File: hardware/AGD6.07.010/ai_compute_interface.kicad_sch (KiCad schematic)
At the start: 12 parts, among them J1 AI_SIGNALS JST-GH 8, J2 AI_OFF_SWITCH JST-GH 2, U2 TPD4E05U06DQA

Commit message: Draw full AGD6.07.010 schematic per integrated_avionics_board spec
All ten sheets now carry components: 14S input with hot-swap and power
monitor, 12/5/3.3 V rails and a separate 12 V AI channel with soft-start
and current telemetry, Pixhawk connectors, CAN1/CAN2 hub with chokes,
ESD and switchable termination, sensor conditioning, SIYI and radar,
AI interface and watchdog, protected 12 V switches with diagnostics,
fan/heater control, cameras and Ethernet. Open choices are recorded in
DECISIONS.md; datasheet-dependent values are flagged CHECK_DATASHEET.

ERC: no errors. All 752 intended pin connections match the KiCad netlist.

Co-Authored-By: Claude Opus 5.5 <noreply@anthropic.com>
Claude-Session: https://claude.ai/code/session_01Qk7uTKdi6YbndB9fGuguYV
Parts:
- removed D1, D2: ESD9B5.0ST5G, Diode_SMD:D_SOD-923, symbol Diode:ESD9B5.0ST5G
- removed J1: AI_SIGNALS JST-GH 8, Connector_JST:JST_GH_SM08B-GHS-TB_1x08-1MP_P1.25mm_Horizontal, symbol Connector_Generic:Conn_01x08
- removed J2: AI_OFF_SWITCH JST-GH 2, Connector_JST:JST_GH_SM02B-GHS-TB_1x02-1MP_P1.25mm_Horizontal, symbol Connector_Generic:Conn_01x02
- removed R1, R2, R3, R4, R5, R9: 100, Resistor_SMD:R_0402_1005Metric, symbol Device:R
- removed R6: 100k, Resistor_SMD:R_0402_1005Metric, symbol Device:R
- removed U2: TPD4E05U06DQA, Package_SON:USON-10_2.5x1.0mm_P0.5mm, symbol Power_Protection:TPD4E05U06DQA
- added D601, D602: ESD9B5.0ST5G, Diode_SMD:D_SOD-923, symbol Diode:ESD9B5.0ST5G
- added J601: AI_SIGNALS GH8, Connector_JST:JST_GH_SM08B-GHS-TB_1x08-1MP_P1.25mm_Horizontal, symbol Connector_Generic:Conn_01x08
- added J602: AI_OFF_SWITCH GH2, Connector_JST:JST_GH_SM02B-GHS-TB_1x02-1MP_P1.25mm_Horizontal, symbol Connector_Generic:Conn_01x02
- added J603: SERVICE USB-C, Connector_USB:USB_C_Receptacle_GCT_USB4105-xx-A_16P_TopMnt_Horizontal, symbol Connector:USB_C_Receptacle_USB2.0_16P
- added J604: AI_USB GH4, Connector_JST:JST_GH_SM04B-GHS-TB_1x04-1MP_P1.25mm_Horizontal, symbol Connector_Generic:Conn_01x04
- added R601, R602, R603, R604, R605, R607: 100, Resistor_SMD:R_0402_1005Metric, symbol Device:R
- added R606: 100k, Resistor_SMD:R_0402_1005Metric, symbol Device:R
- added R608, R609: 5.1k, Resistor_SMD:R_0402_1005Metric, symbol Device:R
- added U602: TPD4E05U06DQA, Package_SON:USON-10_2.5x1.0mm_P0.5mm, symbol Power_Protection:TPD4E05U06DQA
- added U603: USBLC6-2SC6, Package_TO_SOT_SMD:SOT-23-6, symbol Power_Protection:USBLC6-2SC6
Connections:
- net AI_PWR_EN: now also R607.1
- net AI_RX: now also R602.1
- net AI_RX_C: now also J601.3 (Pin_3), R602.2, U602.2 (D1-)
- net AI_TX: now also R601.2
- net AI_TX_C: now also J601.2 (Pin_2), R601.1, U602.1 (D1+)
- net AI_WDI: now also R604.2
- net AI_WD_ARM: now also R605.2, R606.1
- net ARM_C: now also D601.1 (A1), J601.7 (Pin_7), R605.1
- net GND: now also D601.2 (A2), D602.2 (A2), J601.1 (Pin_1), J601.4 (Pin_4), J601.8 (Pin_8), J602.2 (Pin_2), J603.A1 (GND), J603.A12 (GND), J603.B1 (GND), J603.B12 (GND), J603.SH (SHIELD), J604.4 (Pin_4), R606.2, R608.2, R609.2, U602.3 (GND), U602.8 (GND), U603.2 (GND)
- net GNSS_PPS: now also R603.1
- net SW_C: now also D602.1 (A1), J602.1 (Pin_1), R607.2
- net WDI_C: now also J601.6 (Pin_6), R604.1, U602.5 (D2-)
- new net CC1: J603.A5 (CC1), R608.1
- new net CC2: J603.B5 (CC2), R609.1
- new net PPS_C2: J601.5 (Pin_5), R603.2, U602.4 (D2+)
- new net USB_DN: J603.A7 (D-), J603.B7 (D-), J604.2 (Pin_2), U603.3 (I/O2), U603.4 (I/O2)
- new net USB_DP: J603.A6 (D+), J603.B6 (D+), J604.3 (Pin_3), U603.1 (I/O1), U603.6 (I/O1)
- new net USB_VBUS: J603.A4 (VBUS), J603.A9 (VBUS), J603.B4 (VBUS), J603.B9 (VBUS), J604.1 (Pin_1), U603.5 (VBUS)
- no-connect marks 4 -> 6
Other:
- note added: "РАЗЪЁМ ИИ-МОДУЛЯ (сменный companion computer, ТЗ п. 3–4), уровни 3.3 V. Питание 12 V — J202 (лист POWER_CONVERSION). J601: 1 GND, 2 AI_TX (ИИ -> TELEM2), 3 AI_RX, 4 GND, 5 PPS, 6 WDI (импульсы ИИ), 7 WD_ARM (ИИ взводит watchdog), 8 GND. Ethernet ИИ: 2 порта — лист ETHERNET. Сервисный USB-C J603 -> USB ИИ J604 (ESD U603). J602: сервисный выключатель ИИ. Замкнут -> AI_PWR_EN = 0 -> ИИ обесточен; ру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"
- note removed: "J2: сервисный выключатель ИИ. Замкнут -> ИИ обесточен (AI_PWR_EN = 0). Подтяжка AI_PWR_EN — на листе WATCHDOG_DIAGNOSTICS."
- note removed: "R6 держит watchdog разоружённым, пока ИИ загружается."
- note removed: "U2: flow-through — трасса проходит через обе площадки канала, NC-выводы не подключать."
- note removed: "РАЗЪЁМ ИИ-МОДУЛЯ (вариант А: Jetson Orin NX / вариант Б: Orin Nano, RK3588), уровни 3.3 V. J1: 1 GND, 2 AI_TX (ИИ -> Pixhawk TELEM2), 3 AI_RX, 4 GND, 5 PPS (GNSS -> ИИ), 6 WDI (импульсы ИИ), 7 WD_ARM (ИИ взводит watchdog после загрузки), 8 GND. Питание ИИ — лист POWER_CONVERSION."

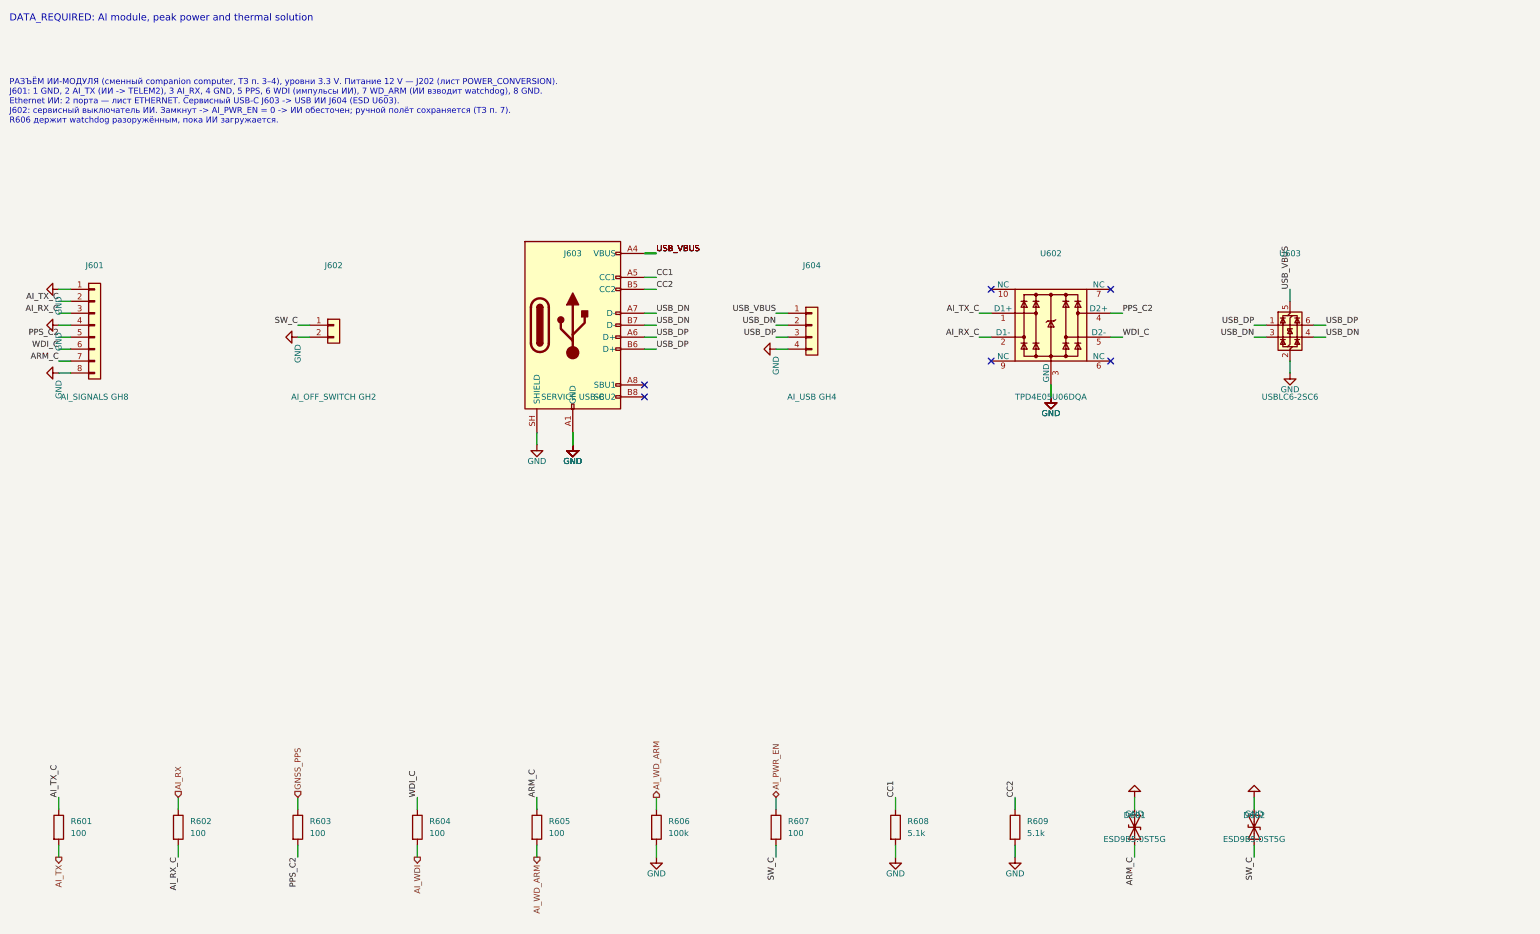
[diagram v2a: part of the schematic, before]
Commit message: AGD6.07.010 rev 0.3: design review fixes and bring-up plan
Design review (DESIGN_REVIEW.md) with fixes applied to the schematic:
INA228 input RC filters, 12 V bus current monitor (INA228 0x45),
BTS5030 diagnostic scaling with clamp diodes, flow input level fix,
CAN1 changed from star to daisy chain with on-board terminator, AI
shutdown request, board buzzer, series resistors and ESD on external
I2C probes. Connectors merged so every connector sits on a board edge.
Adds calculations.md (power, IPC-2221 widths, hot-swap, thermal, ADC
scaling, CAN, clearances) and BRINGUP.md (step-by-step test plan).
ERC: no errors; all 820 intended pin connections verified. Board is
re-placed; routing in progress.

Co-Authored-By: Claude Opus 5.5 <noreply@anthropic.com>
Claude-Session: https://claude.ai/code/session_01Qk7uTKdi6YbndB9fGuguYV
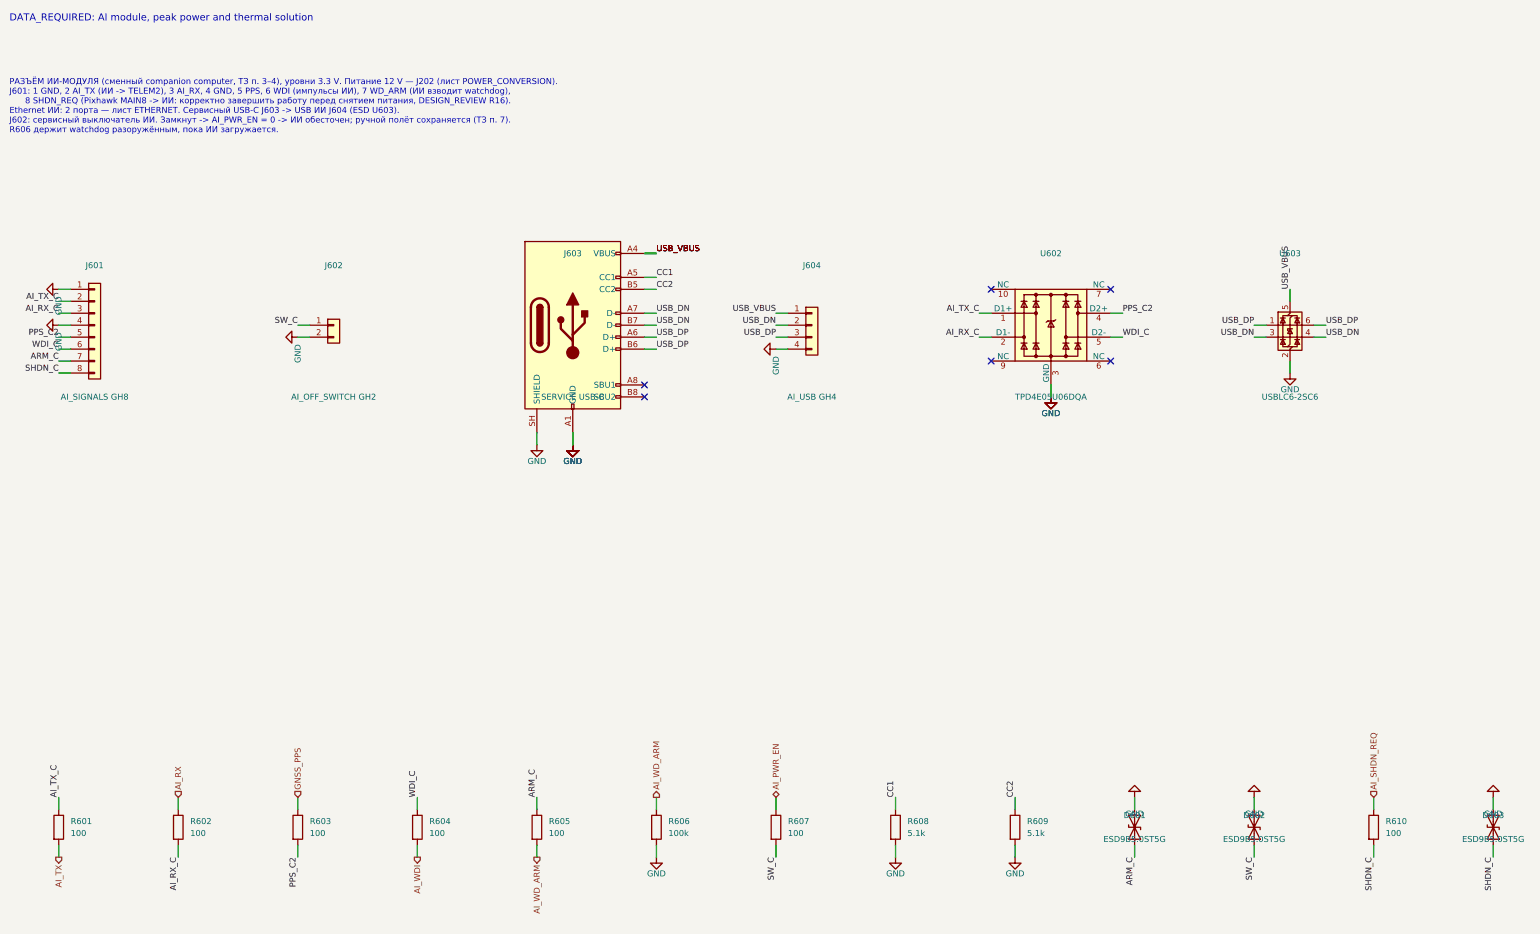
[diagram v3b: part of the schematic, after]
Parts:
- added D603: ESD9B5.0ST5G, Diode_SMD:D_SOD-923, symbol Diode:ESD9B5.0ST5G
- added R610: 100, Resistor_SMD:R_0402_1005Metric, symbol Device:R
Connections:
- net GND: now also D603.2 (A2); no longer J601.8 (Pin_8)
- new net AI_SHDN_REQ: R610.1
- new net SHDN_C: D603.1 (A1), J601.8 (Pin_8), R610.2
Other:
- note added: "РАЗЪЁМ ИИ-МОДУЛЯ (сменный companion computer, ТЗ п. 3–4), уровни 3.3 V. Питание 12 V — J202 (лист POWER_CONVERSION). J601: 1 GND, 2 AI_TX (ИИ -> TELEM2), 3 AI_RX, 4 GND, 5 PPS, 6 WDI (импульсы ИИ), 7 WD_ARM (ИИ взводит watchdog), 8 SHDN_REQ (Pixhawk MAIN8 -> ИИ: корректно завершить работу перед снятием питания, DESIGN_REVIEW R16). Ethernet ИИ: 2 порта — лист ETHERNET. Сервисный USB-C J603 -> USB 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"
- note removed: "РАЗЪЁМ ИИ-МОДУЛЯ (сменный companion computer, ТЗ п. 3–4), уровни 3.3 V. Питание 12 V — J202 (лист POWER_CONVERSION). J601: 1 GND, 2 AI_TX (ИИ -> TELEM2), 3 AI_RX, 4 GND, 5 PPS, 6 WDI (импульсы ИИ), 7 WD_ARM (ИИ взводит watchdog), 8 GND. Ethernet ИИ: 2 порта — лист ETHERNET. Сервисный USB-C J603 -> USB ИИ J604 (ESD U603). J602: сервисный выключатель ИИ. Замкнут -> AI_PWR_EN = 0 -> ИИ обесточен; ру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"

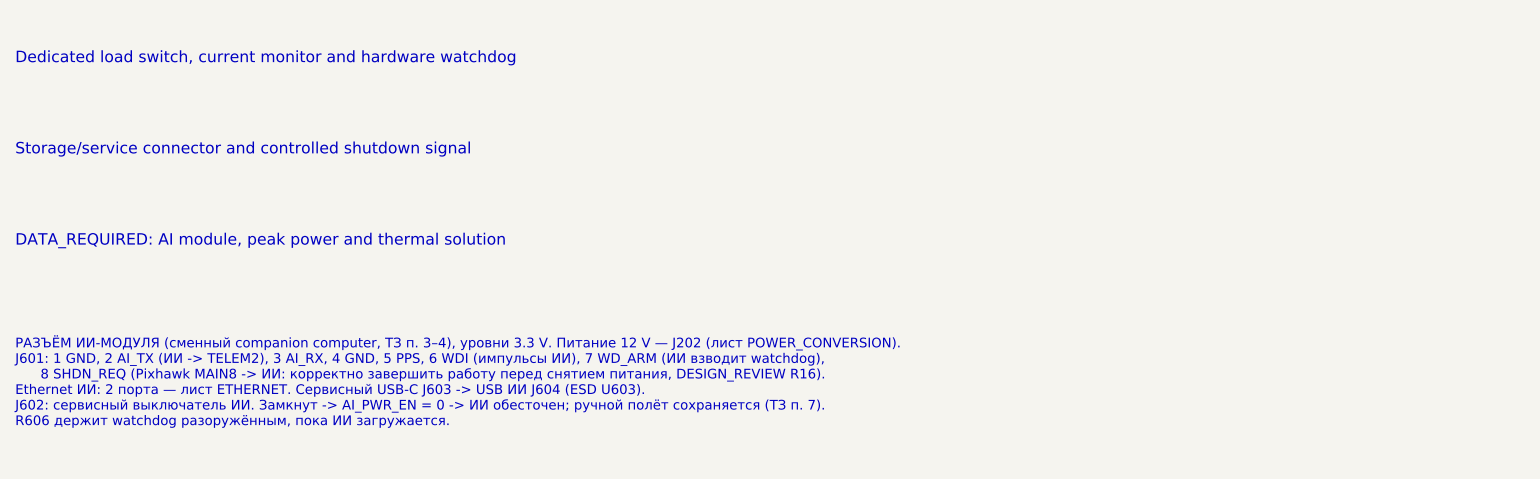
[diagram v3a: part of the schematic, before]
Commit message: AGD6.07.010: AI computer RK3588 - PS202 = TEP 75-4812WI, RS201 10 mOhm, docs and outputs updated
Co-Authored-By: Claude Opus 5.5 <noreply@anthropic.com>
Claude-Session: https://claude.ai/code/session_01Qk7uTKdi6YbndB9fGuguYV
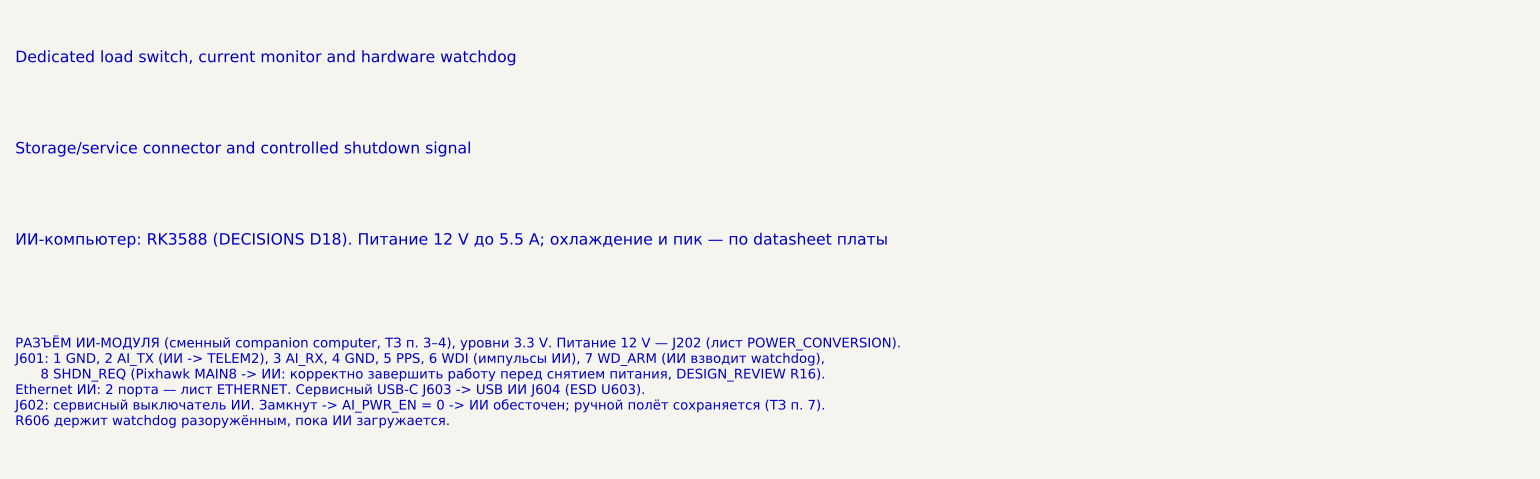
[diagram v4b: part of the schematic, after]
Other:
- note added: "ИИ-компьютер: RK3588 (DECISIONS D18). Питание 12 V до 5.5 A; охлаждение и пик — по datasheet платы"
- note removed: "DATA_REQUIRED: AI module, peak power and thermal solution"

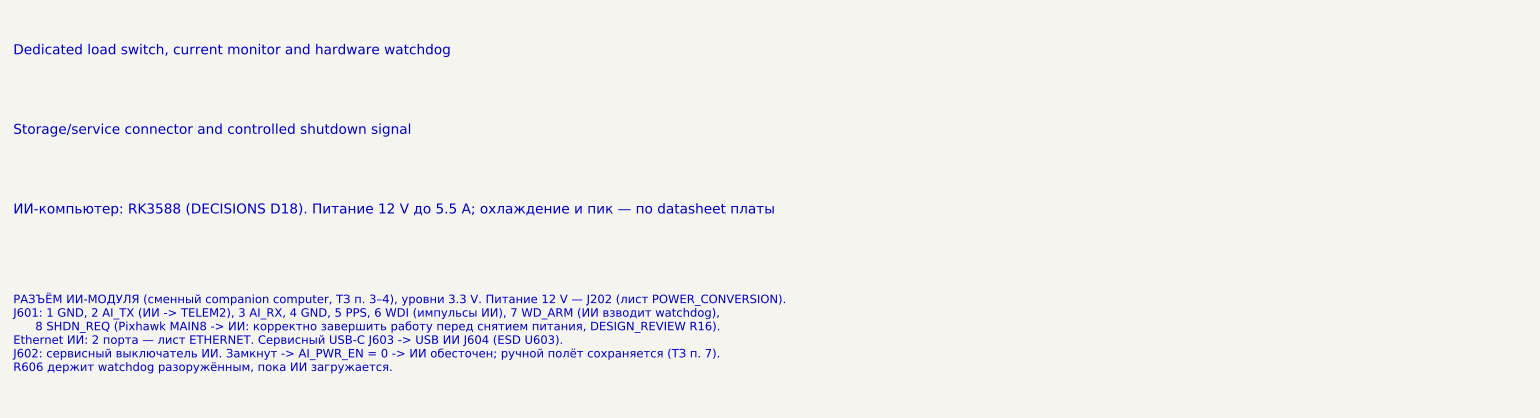
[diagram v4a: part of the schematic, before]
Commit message: AGD6.07.010: AI computer Firefly RK3588 (ROC-RK3588S-PC), power harness and interface notes
Co-Authored-By: Claude Opus 5.5 <noreply@anthropic.com>
Claude-Session: https://claude.ai/code/session_01Qk7uTKdi6YbndB9fGuguYV
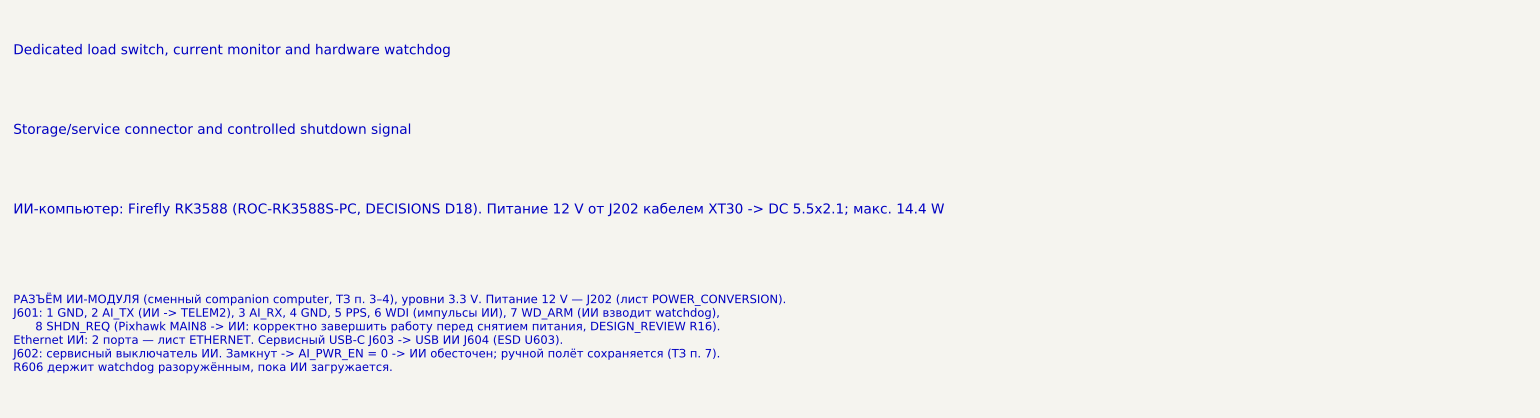
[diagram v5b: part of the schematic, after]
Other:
- note added: "ИИ-компьютер: Firefly RK3588 (ROC-RK3588S-PC, DECISIONS D18). Питание 12 V от J202 кабелем XT30 -> DC 5.5x2.1; макс. 14.4 W"
- note removed: "ИИ-компьютер: RK3588 (DECISIONS D18). Питание 12 V до 5.5 A; охлаждение и пик — по datasheet платы"
